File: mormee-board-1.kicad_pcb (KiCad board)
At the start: 4 copper layers, 40 x 60 mm, 152 parts, among them J2 24FLZ-SM2-TB, J3 USB4105-GF-A, J4 S2B-PH-SM4-TB_LF__SN_, J5 DM3BT-DSF-PEJS, M1 IMP34DT05TR, M2 IMP34DT05TR, Q1 AO3401A, SW1 EVQ-PUB02K, SW2 EVQ-PUB02K, U1 W25Q128JVSIQ, U10 MAX17048G+T10, U11 MP2637GR-P, U2 RTL8735BDM-A20-N04, U3 FDS9926A, U4 FT232RNL-REEL, U5 RT8097AHGE, U6 RT8097AHGE, U7 RT9080-28GJ5, U8 RT9080-18GJ5, U9 RT9080-12GJ5

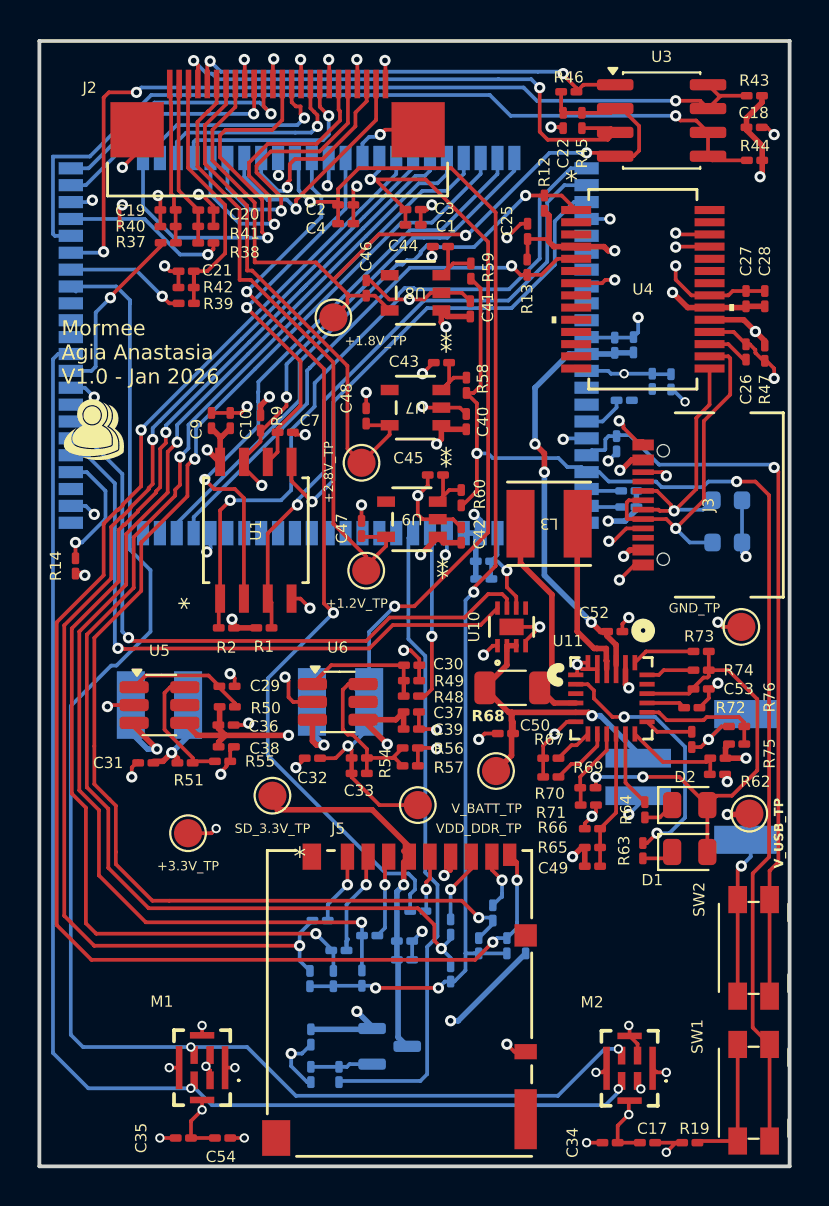
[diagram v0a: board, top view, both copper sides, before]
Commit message: Added mounting holes and alignment notches
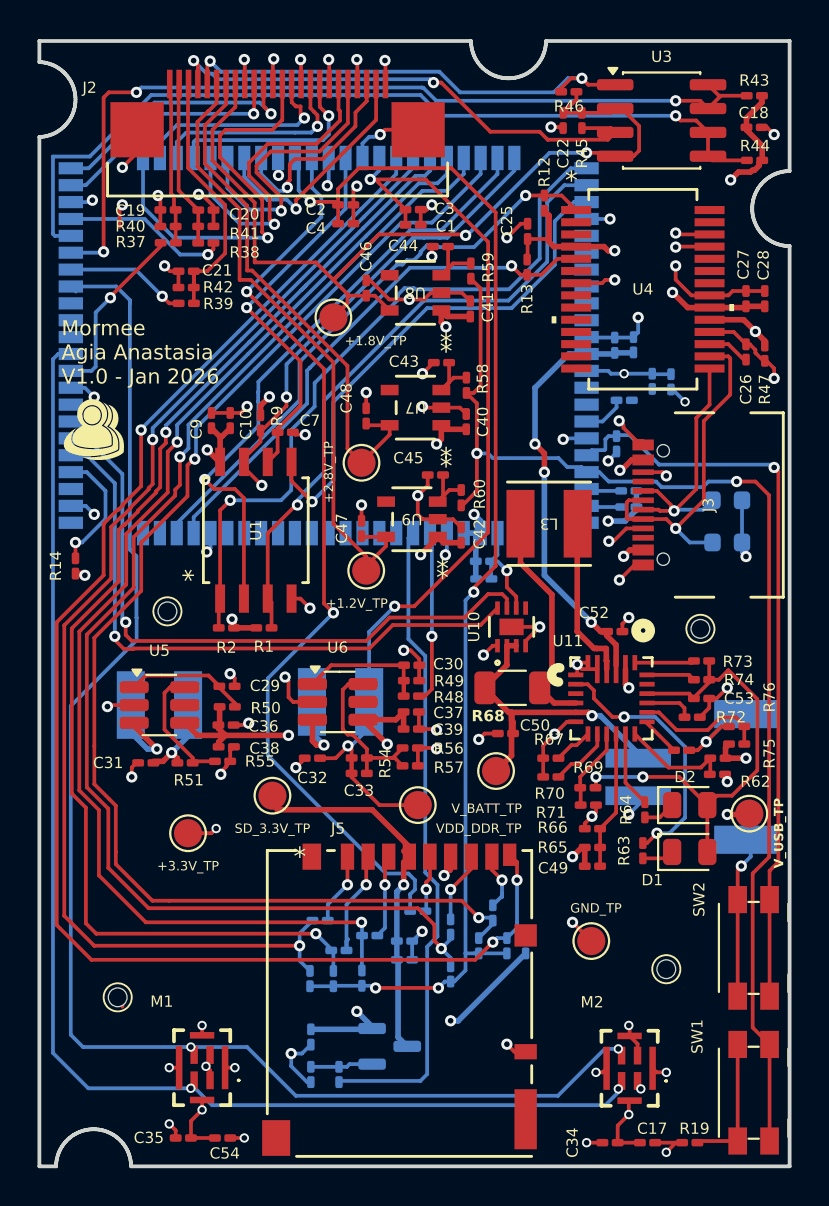
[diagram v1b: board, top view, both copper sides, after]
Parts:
- added REF**: MountingHole_1mm, Alignment:MountingHole_1mm, F.Cu at (102.8, 90.2)
- added REF**: MountingHole_1mm, Alignment:MountingHole_1mm, F.Cu at (73.5, 91.8)
- added REF**: MountingHole_1mm, Alignment:MountingHole_1mm, F.Cu at (76.2, 71.2)
- added REF**: MountingHole_1mm, Alignment:MountingHole_1mm, F.Cu at (104.6, 72.1)
- moved TP9 18.6 mm to (98.8, 88.8), turned to 90 degrees
- moved C51 0.79 mm to (103.6, 78.6), turned to 0 degrees
- moved C53 0.51 mm to (104.6, 75.8)
- moved R72 0.51 mm to (104.1, 76.8)
- moved R73 0.51 mm to (104.6, 73.8)
- moved R74 0.51 mm to (104.6, 74.8)
- turned R46 to 180 degrees
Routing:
- net /SD CARD /Vidio / Audio / USB/SDA: track 23.5 -> 25.5 mm
- net /SD CARD /Vidio / Audio / USB/SCL: track 29.0 -> 27.6 mm
- net +3.3V: track 65.9 -> 67.2 mm
- net GND: track 167.2 -> 168.3 mm
- net DMIC_CLK: track 78.0 -> 77.2 mm
- net Net-(U11-ILIM): track 2.08 -> 2.60 mm
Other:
- outline, holes or cut-outs redrawn

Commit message: Ready. I think. At last. Probably.
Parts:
- added F1: Fiducial_0.75mm_Mask1.5mm, Fiducial:Fiducial_0.75mm_Mask1.5mm, F.Cu at (107.5, 43.2)
- added F2: Fiducial_0.75mm_Mask1.5mm, Fiducial:Fiducial_0.75mm_Mask1.5mm, F.Cu at (72.2, 97.0)
- added F3: Fiducial_0.75mm_Mask1.5mm, Fiducial:Fiducial_0.75mm_Mask1.5mm, F.Cu at (100.8, 91.0)
- added F4: Fiducial_0.75mm_Mask1.5mm, Fiducial:Fiducial_0.75mm_Mask1.5mm, B.Cu at (106.2, 43.8)
- added F5: Fiducial_0.75mm_Mask1.5mm, Fiducial:Fiducial_0.75mm_Mask1.5mm, B.Cu at (106.0, 96.8)
- added F6: Fiducial_0.75mm_Mask1.5mm, Fiducial:Fiducial_0.75mm_Mask1.5mm, B.Cu at (74.2, 88.0)
- added LF1: Fiducial_0.75mm_Mask1.5mm, Fiducial:Fiducial_0.75mm_Mask1.5mm, B.Cu at (101.8, 47.5)
- added LF2: Fiducial_0.75mm_Mask1.5mm, Fiducial:Fiducial_0.75mm_Mask1.5mm, B.Cu at (71.8, 69.2)
- moved R44 1.75 mm to (105.9, 48.0)
- moved MH3 1.52 mm to (102.5, 88.8)
- moved R43 1.33 mm to (107.2, 45.0)
- moved TP1 1.25 mm to (76.0, 83.0)
- moved C13 0.75 mm to (88.8, 89.5)
- moved C14 0.75 mm to (88.8, 90.5)
- moved C18 0.66 mm to (107.2, 46.0), turned to 180 degrees
- moved TP4 0.56 mm to (89.0, 81.2)
- moved TP6 0.21 mm to (81.7, 81.2)
- renumbered REF** to MH1, REF** to MH2, REF** to MH3, REF** to MH4
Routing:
- net +3.3V: track 67.2 -> 65.4 mm
- net SEN_SCL: track 45.7 -> 44.8 mm
- net DMIC_DATA: track 70.8 -> 70.0 mm
- net Net-(J5-CD/DAT3): track 6.11 -> 5.48 mm
- net GND: track 168.3 -> 167.9 mm, vias 84 -> 83
